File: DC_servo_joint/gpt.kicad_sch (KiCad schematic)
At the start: 41 parts, among them U1 AS5600, U2 ESP32-C3-WROOM-02, U3 SP3485EN, U5 TPS563200

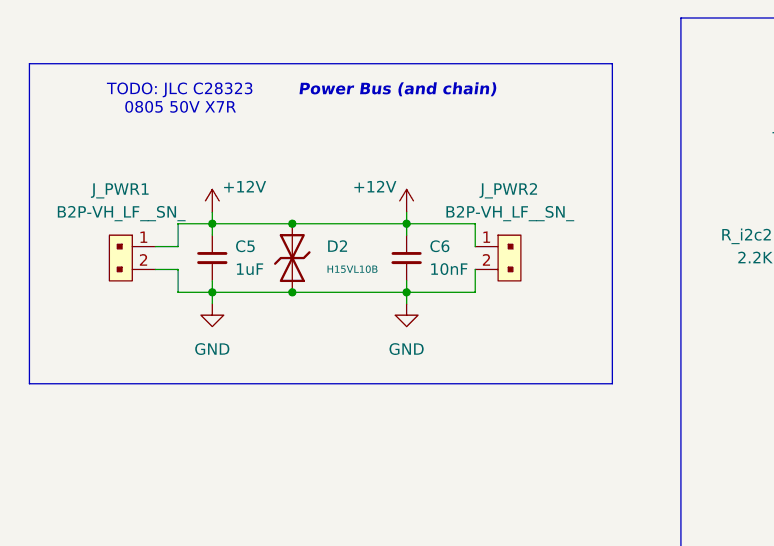
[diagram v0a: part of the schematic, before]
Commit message: Change to JST VH connector for power
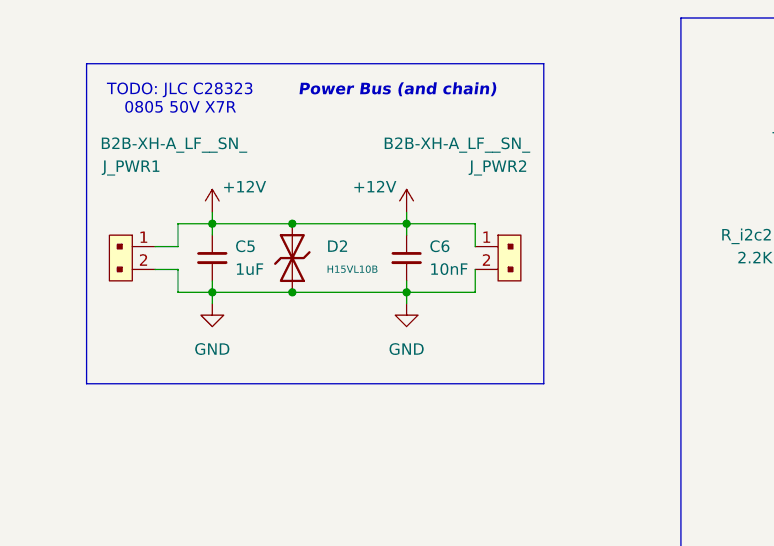
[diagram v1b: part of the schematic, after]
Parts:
- removed J_PWR1, J_PWR2: B2P-VH_LF__SN_, digikey-footprints:PinHeader_1x2_P3.96mm_Drill1.6mm, symbol dk_Rectangular-Connectors-Headers-Male-Pins:B2P-VH_LF__SN_
- added J_PWR1, J_PWR2: B2B-XH-A_LF__SN_, digikey-footprints:PinHeader_1x2_P2.5mm_Drill1.1mm, symbol dk_Rectangular-Connectors-Headers-Male-Pins:B2B-XH-A_LF__SN_
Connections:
- net +12V: now also J_PWR1.1, J_PWR2.1
- net GND: now also J_PWR1.2, J_PWR2.2
